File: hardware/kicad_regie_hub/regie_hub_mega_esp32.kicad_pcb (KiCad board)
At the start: 2 copper layers, 180 x 140 mm, 12 parts

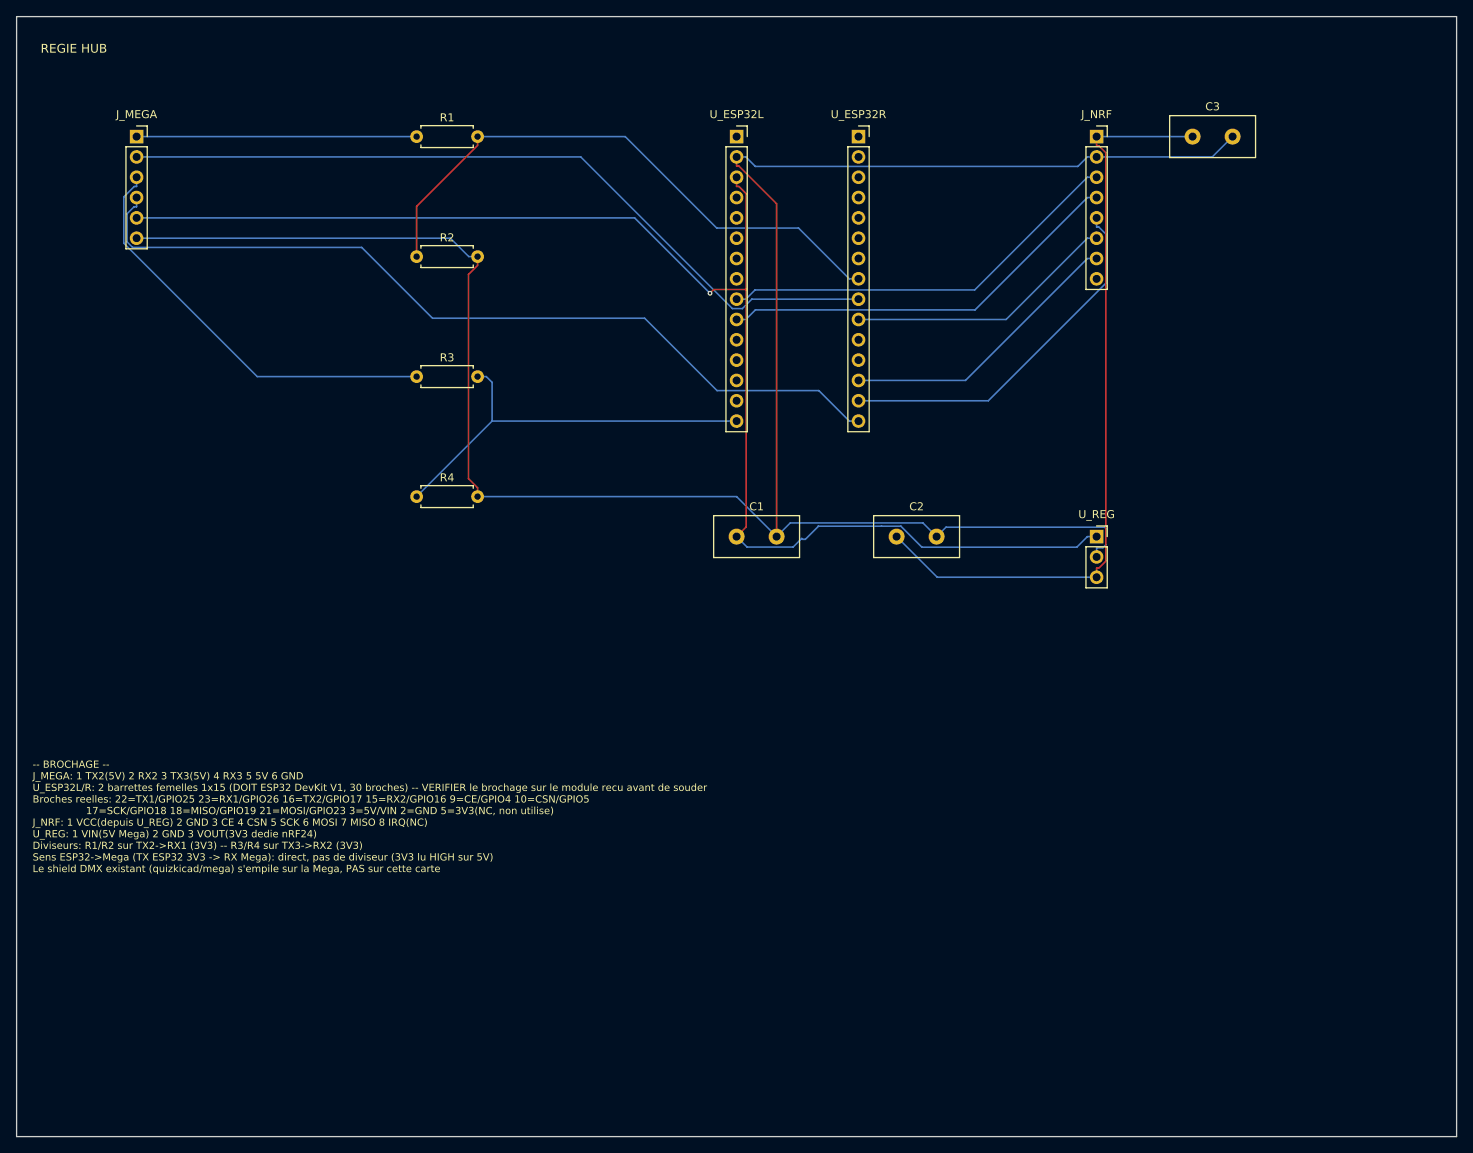
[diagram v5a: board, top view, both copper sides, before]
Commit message: hardware: corrige VCC/GND nRF24 (inverses) + passe en 2x4 (module PA+LNA)
En reponse a "le nrf24 c'est sur une ligne ?", verification du brochage
nRF24 contre 3 sources independantes (components101.com,
lastminuteengineers.com, doc generale nRF24L01+) : la broche 1 est GND et
la broche 2 est VCC, pas l'inverse comme c'etait cable jusqu'ici sur J1
(carte Nano) et J_NRF (carte hub) -- schema ET PCB. Broche 1 = toujours la
pastille carree sur cette empreinte, coherent avec "GND identifiable par
son marquage carre" documente pour ce module.

Le module confirme etant un nRF24L01+PA+LNA (longue portee), son connecteur
est 2x4 et non 1x8 standard -- empreinte changee vers PinSocket_2x04 sur
les 2 cartes concernees, brochage 1=GND 2=VCC puis CE/CSN/SCK/MOSI/MISO/IRQ
sur les rangees suivantes (ordre le plus courant publie, mais AUCUN
standard universel n'existe pour les variantes PA+LNA -- avertissement
explicite dans le README et sur la serigraphie: verifier sur le module
recu avant de souder).

Schemas re-verifies (kicad-cli sch erc, memes comptes qu'avant -- aucune
regression). PCB re-routes (Freerouting) et revalides (kicad-cli pcb drc):
0 violation de clearance, 0 element non connecte, 0 track_dangling.

Co-Authored-By: Claude Sonnet 5 <noreply@anthropic.com>
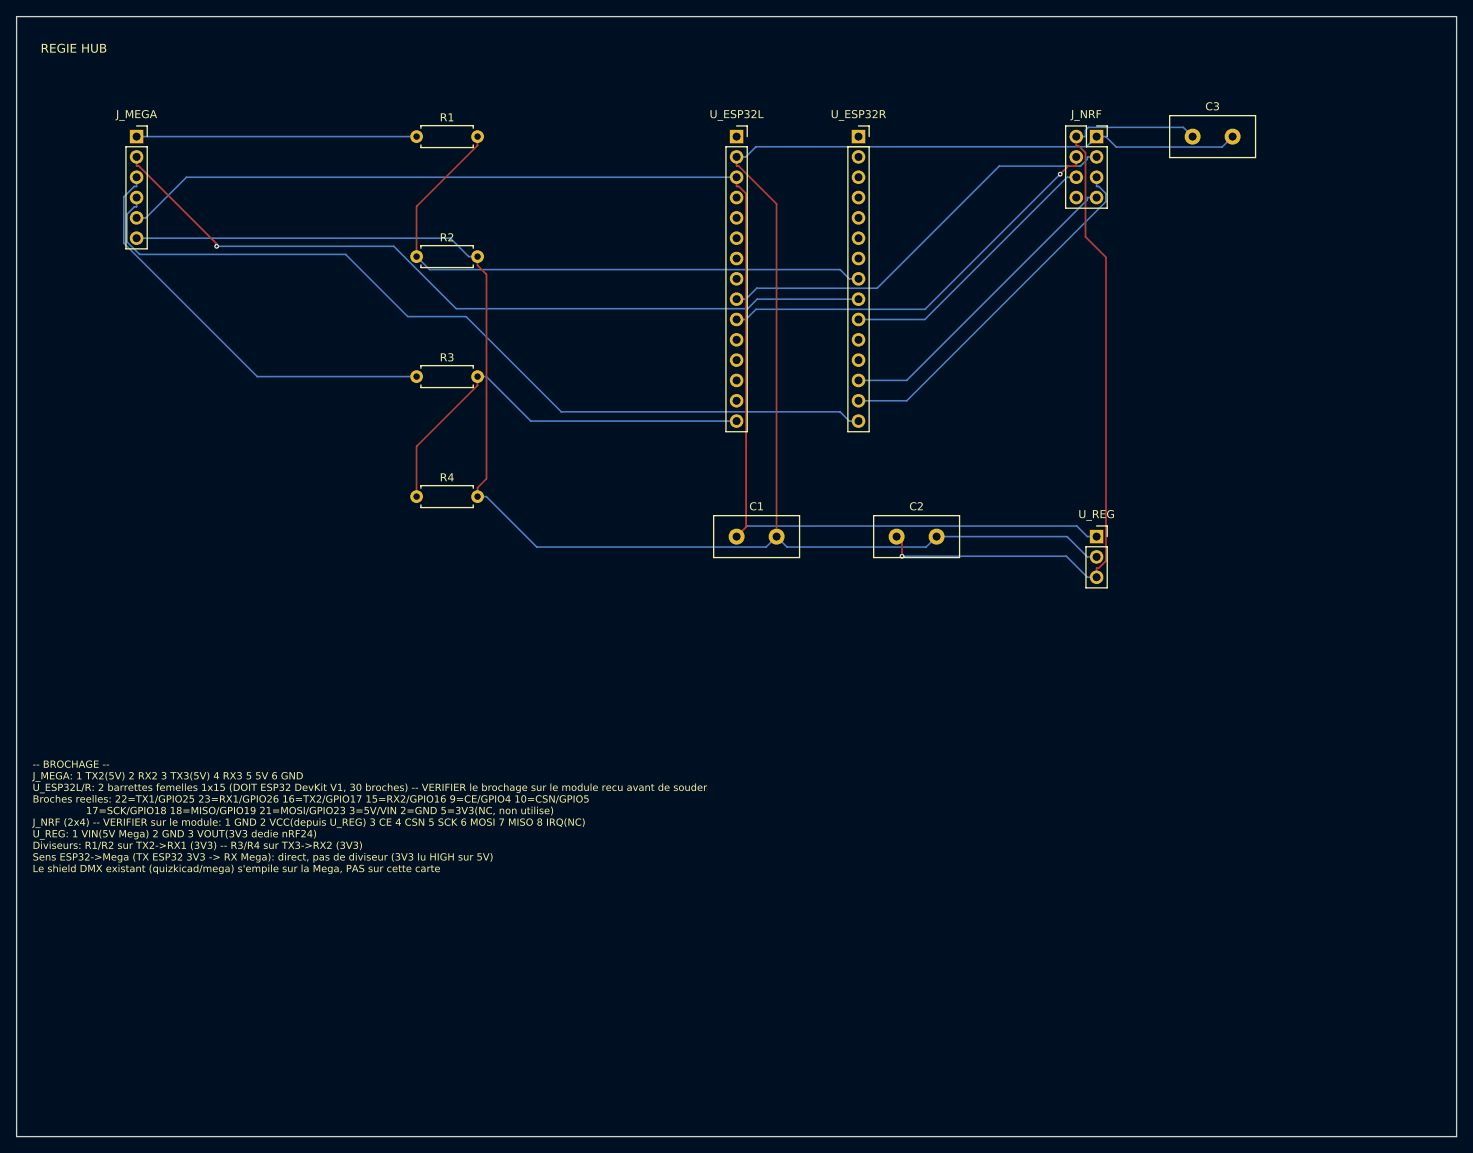
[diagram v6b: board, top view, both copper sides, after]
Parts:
- removed the J_NRF at (140.0, 20.0)
- added J_NRF: nRF24L01+PA+LNA - VERIFIER le brochage sur le module recu, Connector_PinSocket_2.54mm:PinSocket_2x04_P2.54mm_Vertical, F.Cu at (140.0, 20.0)
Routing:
- net NRF_VCC_DEDIE: track 95.5 -> 101.5 mm, vias 0 -> 1
- net VCC_5V_MEGA: track 174.7 -> 169.3 mm, vias 1 -> 0
- net GND: track 275.3 -> 271.0 mm
- net NRF_MISO: track 36.1 -> 39.4 mm
- net ESP32_RX2_3V3: track 50.9 -> 52.8 mm
- net ESP32_RX1_3V3: track 73.1 -> 74.5 mm
- net NRF_CE: track 51.3 -> 52.5 mm
- net NRF_SCK: track 45.8 -> 44.9 mm
- net MEGA_RX2_DIRECT: track 98.6 -> 99.4 mm, vias 0 -> 1
- net NRF_MOSI: track 34.0 -> 34.6 mm
- net NRF_CSN: track 51.3 -> 51.6 mm, vias 0 -> 1
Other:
- board text added: "-- BROCHAGE -- J_MEGA: 1 TX2(5V) 2 RX2 3 TX3(5V) 4 RX3 5 5V 6 GND U_ESP32L/R: 2 barrettes femelles 1x15 (DOIT ESP32 DevKit V1, 30 broches) -- VERIFIER le brochage sur le module recu avant de souder Broches reelles: 22=TX1/GPIO25 23=RX1/GPIO26 16=TX2/GPIO17 15=RX2/GPIO16 9=CE/GPIO4 10=CSN/GPIO5 17=SCK/GPIO18 18=MISO/GPIO19 21=MOSI/GPIO23 3=5V/VIN 2=GND 5=3V3(NC, non utilise) J_NRF (2x4) -- VERIFIE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"
- board text removed: "-- BROCHAGE -- J_MEGA: 1 TX2(5V) 2 RX2 3 TX3(5V) 4 RX3 5 5V 6 GND U_ESP32L/R: 2 barrettes femelles 1x15 (DOIT ESP32 DevKit V1, 30 broches) -- VERIFIER le brochage sur le module recu avant de souder Broches reelles: 22=TX1/GPIO25 23=RX1/GPIO26 16=TX2/GPIO17 15=RX2/GPIO16 9=CE/GPIO4 10=CSN/GPIO5 17=SCK/GPIO18 18=MISO/GPIO19 21=MOSI/GPIO23 3=5V/VIN 2=GND 5=3V3(NC, non utilise) J_NRF: 1 VCC(depuis U_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"

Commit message: hardware: cartes retrecies, guide serigraphie retire, keepout sous le nRF24
3 demandes traitees sur les 3 cartes:

- Retrait du texte-guide en serigraphie (bloc BROCHAGE) -- n'a plus sa
  place sur un circuit destine a la fabrication reelle. Repere de
  composant standard (A1L, J1, C1...) conserve, paragraphe d'instructions
  retire.
- Cartes nettement plus compactes: nano 125x145 -> 90x100mm, hub
  185x145 -> 137x85mm, esp32 130x145 -> 68x101mm.
- Nano/hub: C1/C3 (decouplage nRF24) rapproches encore plus de J1/J_NRF.
- Zone sans cuivre (keepout, pistes/vias/plans interdits sur F.Cu ET B.Cu)
  ajoutee sous l'emplacement du module nRF24 PA+LNA sur les 2 cartes qui en
  ont un (nano, hub) -- pas de cuivre sous l'antenne du module. Verifie
  reellement respecte par Freerouting (pas juste accepte par kicad-cli):
  un test dedie avec un keepout bloquant deliberement le seul chemin entre
  2 pastilles a fait router 0 piste par l'autorouteur, preuve qu'il n'etait
  pas ignore. Premiere disposition (keepout collant a J1 sur plusieurs
  cotes) a bloque le routeur (8 pistes indefiniment non routees apres 100+
  passes) -- corrige en placant le keepout en presqu'ile contre le bord de
  la carte, ne bloquant aucun chemin de routage necessaire.

Les 3 cartes re-routees (Freerouting) et revalidees (kicad-cli pcb drc):
0 violation de clearance, 0 element non connecte, 0 track_dangling sur les
3, et 0 piste a l'interieur des zones keepout (verifie par script).

Co-Authored-By: Claude Sonnet 5 <noreply@anthropic.com>
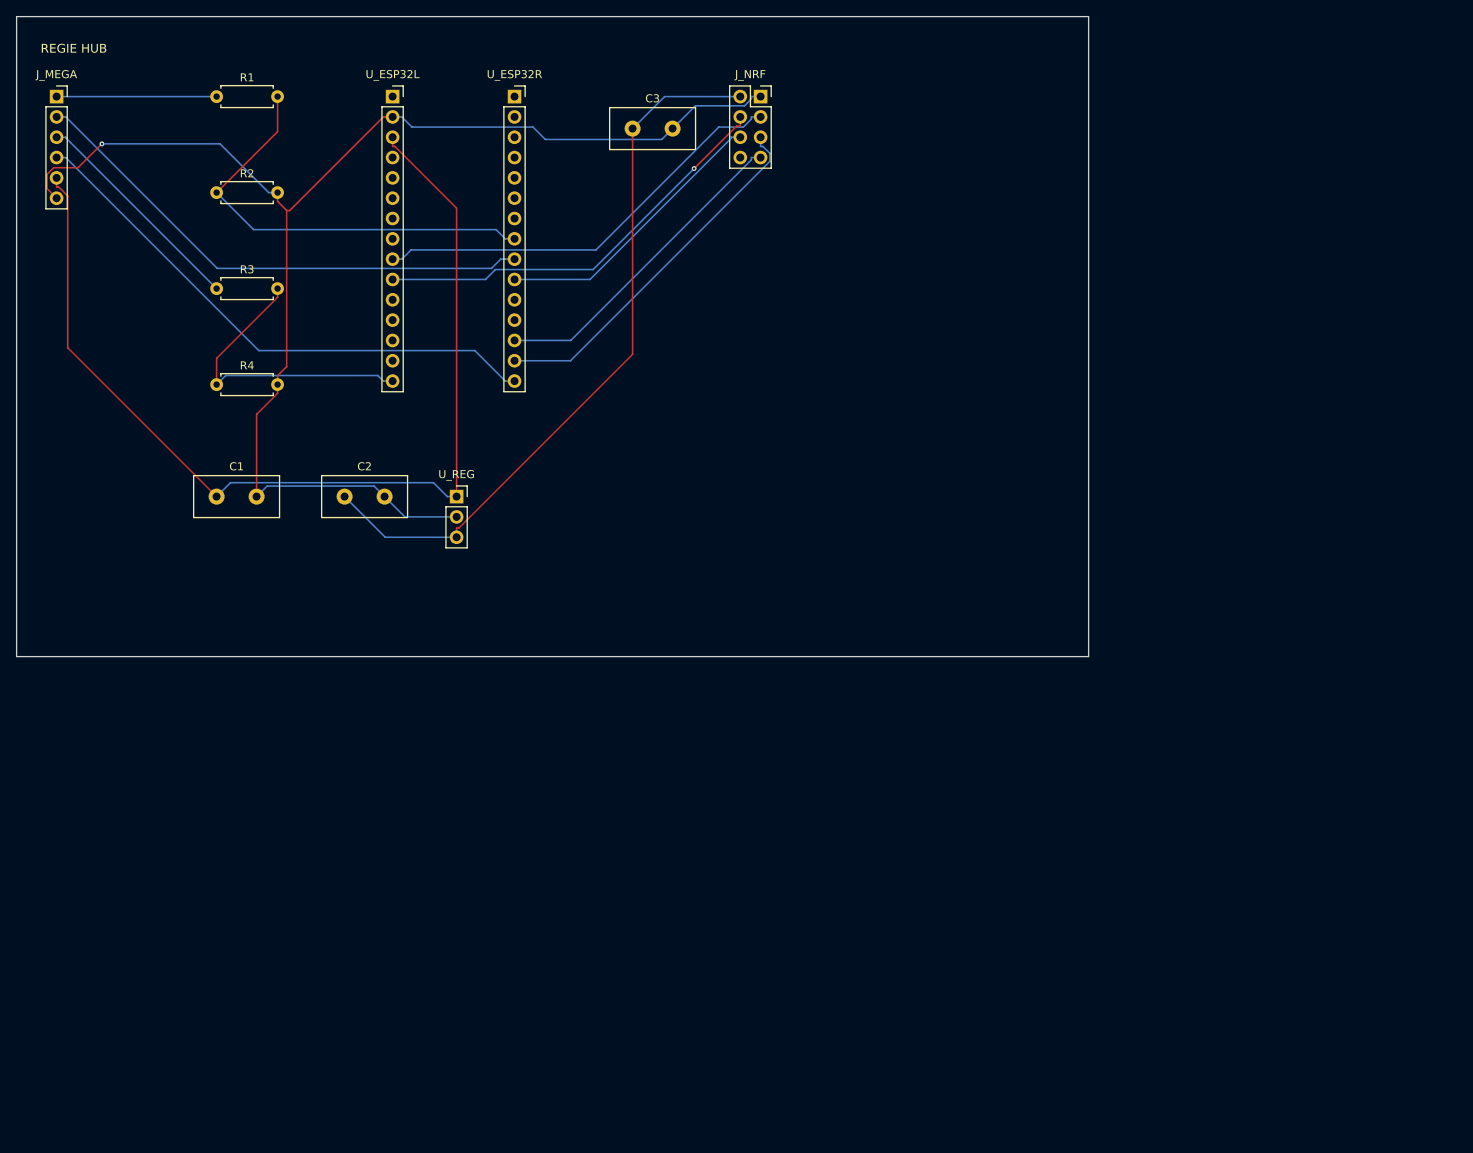
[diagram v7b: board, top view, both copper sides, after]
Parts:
- C3: value 10-100uF decouplage nRF24 (obligatoire) -> 10-100uF decouplage nRF24 (obligatoire, au plus pres)
- moved U_REG 80.2 mm to (60.0, 65.0)
- moved C3 70.0 mm to (82.0, 19.0)
- moved C2 69.2 mm to (46.0, 65.0)
- moved C1 65.2 mm to (30.0, 65.0)
- moved U_ESP32L 43.3 mm to (52.0, 15.0)
- moved U_ESP32R 43.3 mm to (67.2, 15.0)
- moved J_NRF 42.3 mm to (98.0, 15.0)
- moved R4 28.7 mm to (30.0, 51.0)
- moved R3 27.3 mm to (30.0, 39.0)
- moved R2 26.2 mm to (30.0, 27.0)
- moved R1 25.5 mm to (30.0, 15.0)
- moved J_MEGA 11.2 mm to (10.0, 15.0)
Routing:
- net GND: track 271.0 -> 171.2 mm, vias 0 -> 1
- net VCC_5V_MEGA: track 169.3 -> 128.1 mm
- net MEGA_RX3_DIRECT: track 106.9 -> 68.8 mm
- net MEGA_RX2_DIRECT: track 99.4 -> 65.6 mm, vias 1 -> 0
- net MEGA_TX3_5V: track 52.6 -> 27.9 mm
- net ESP32_RX1_3V3: track 74.5 -> 54.8 mm
- net MEGA_TX2_5V: track 35.0 -> 20.0 mm
- net ESP32_RX2_3V3: track 52.8 -> 37.9 mm
- net NRF_VCC_DEDIE: track 101.5 -> 91.6 mm, vias 1 -> 0
- net NRF_MOSI: track 34.6 -> 35.7 mm
- net NRF_MISO: track 39.4 -> 40.4 mm
- net NRF_CSN: track 51.6 -> 52.6 mm
- net NRF_SCK: track 44.9 -> 45.9 mm
- net NRF_CE: track 52.5 -> 53.5 mm
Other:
- board size 180 x 140 mm -> 134 x 80 mm
- board text removed: "-- BROCHAGE -- J_MEGA: 1 TX2(5V) 2 RX2 3 TX3(5V) 4 RX3 5 5V 6 GND U_ESP32L/R: 2 barrettes femelles 1x15 (DOIT ESP32 DevKit V1, 30 broches) -- VERIFIER le brochage sur le module recu avant de souder Broches reelles: 22=TX1/GPIO25 23=RX1/GPIO26 16=TX2/GPIO17 15=RX2/GPIO16 9=CE/GPIO4 10=CSN/GPIO5 17=SCK/GPIO18 18=MISO/GPIO19 21=MOSI/GPIO23 3=5V/VIN 2=GND 5=3V3(NC, non utilise) J_NRF (2x4) -- VERIFIE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"

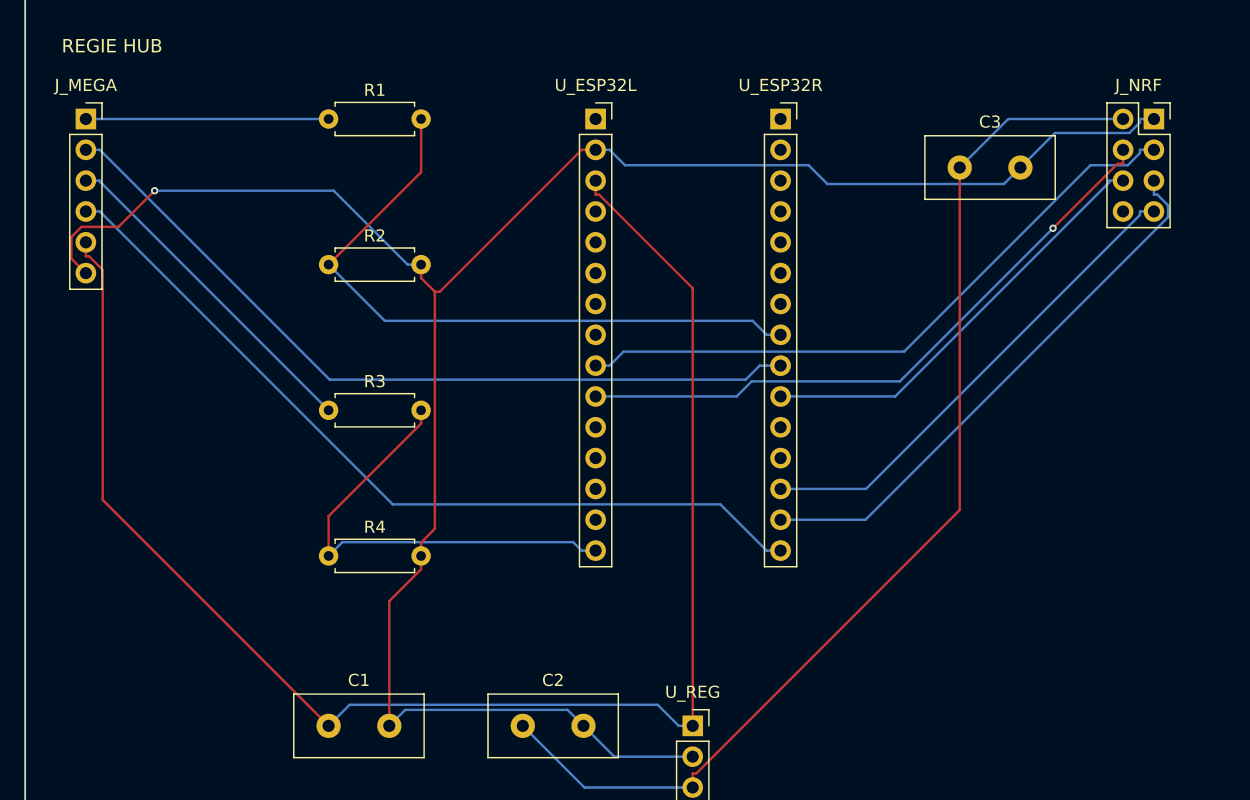
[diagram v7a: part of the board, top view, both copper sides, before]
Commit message: hardware: J1/J_NRF en broches males (le module nRF24 a des ports femelles)
Le module nRF24L01+PA+LNA a lui-meme des ports femelles sur son connecteur
2x4 -- l'empreinte utilisee jusqu'ici (PinSocket_2x04, femelle cote carte)
etait donc a l'envers. Change en PinHeader_2x04 (broches MALES) sur les 2
cartes concernees (nano, hub), pour que le module s'enfiche directement
dessus -- logique inverse de A1L/A1R (Nano) et U_ESP32L/R ou U1L/U1R (ESP32)
dont les modules ont eux-memes des broches males.

Le footprint male a son empreinte MIROIR par rapport au femelle (pastille 2
a +2.54mm au lieu de -2.54mm) -- numerotation de broche inchangee (1=GND,
2=VCC... comme deja verifie), seule la position physique change. Ajuste de
quelques mm la position de J1/J_NRF et de la zone keepout pour garder le
meme espacement de securite avec le nouveau contour de composant.

Les 2 cartes re-routees (Freerouting) et revalidees (kicad-cli pcb drc):
0 violation de clearance, 0 element non connecte, 0 piste dans la zone
keepout (verifie par script), 0 track_dangling apres nettoyage des residus
d'autorouter habituels sur la carte hub.

Co-Authored-By: Claude Sonnet 5 <noreply@anthropic.com>
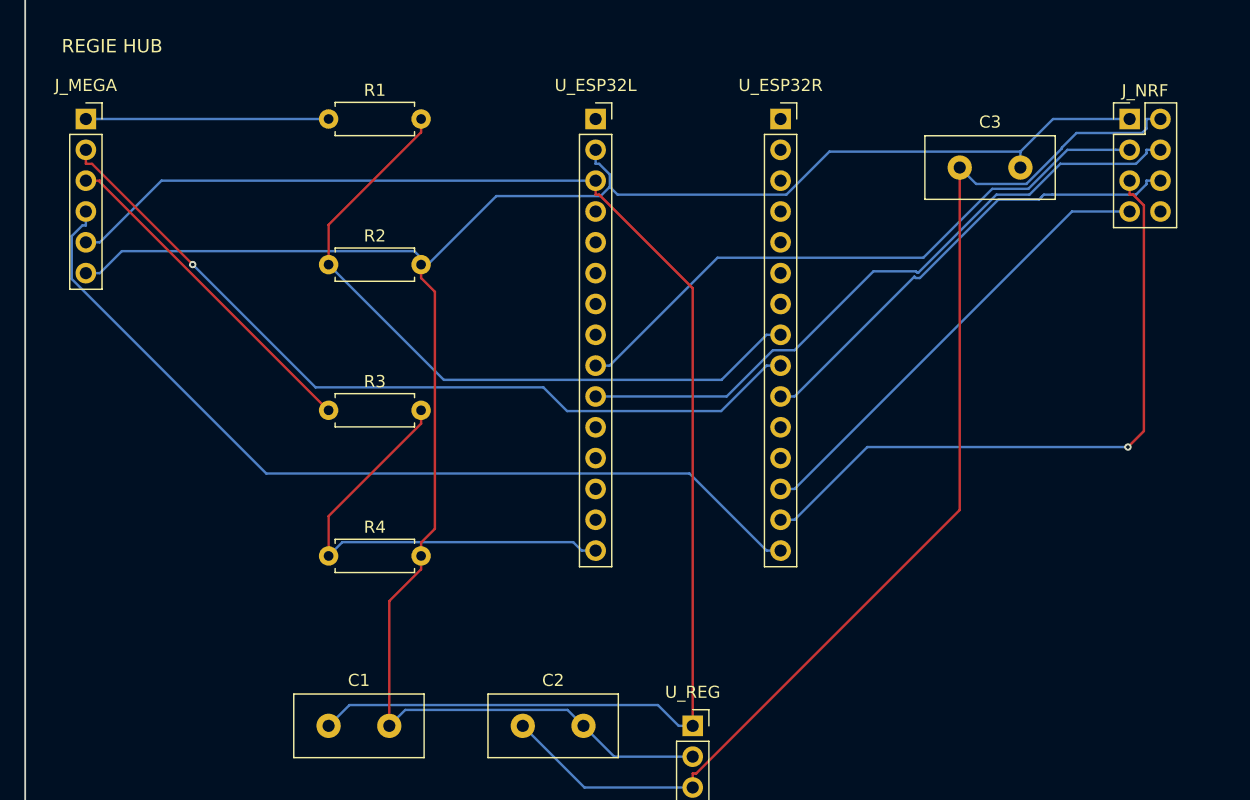
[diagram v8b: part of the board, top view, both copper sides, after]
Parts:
- removed the J_NRF at (98.0, 15.0)
- added J_NRF: nRF24L01+PA+LNA (broches MALES, le module a des ports femel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, Connector_PinHeader_2.54mm:PinHeader_2x04_P2.54mm_Vertical, F.Cu at (96.0, 15.0)
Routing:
- net NRF_SCK: track 45.9 -> 54.3 mm, vias 0 -> 1
- net GND: track 171.2 -> 165.4 mm, vias 1 -> 0
- net MEGA_RX3_DIRECT: track 68.8 -> 73.9 mm
- net NRF_VCC_DEDIE: track 91.6 -> 96.3 mm
- net VCC_5V_MEGA: track 128.1 -> 123.9 mm
- net NRF_MOSI: track 35.7 -> 38.9 mm
- net ESP32_RX1_3V3: track 54.8 -> 57.9 mm
- net MEGA_RX2_DIRECT: track 65.6 -> 68.4 mm, vias 0 -> 1
- net NRF_CSN: track 52.6 -> 55.2 mm, vias 1 -> 0
- net NRF_MISO: track 40.4 -> 38.2 mm
- net NRF_CE: track 53.5 -> 51.4 mm
